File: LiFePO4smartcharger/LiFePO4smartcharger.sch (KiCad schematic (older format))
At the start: 96 parts, among them J1 Conn_01x02, J10 Conn_01x01, J11 Conn_01x01, J12 Conn_01x04, J2 Conn_02x03_Odd_Even, J3 Conn_01x02, J4 Conn_01x02, J5 Barrel_Jack, J6 Conn_01x01, J7 Conn_01x01, J8 Conn_01x02, J9 Conn_01x02, Q1 TIP42, Q2 TIP41, Q4 TIP41C, T1 Transformer_1P1Sdotted, U1 ATMEGA328P-PU, U2 LM358, U3 LCD-016N002L, U4 TL494, U9 LM7805_TO220, X3 16MHz

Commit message: Added important shutdown feature
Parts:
- added D8: 1N4148, Diodes_THT:D_DO-35_SOD27_P7.62mm_Horizontal, symbol D
- D4: footprint (none) -> Diodes_THT:D_DO-41_SOD81_P7.62mm_Horizontal
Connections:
- net CURRENTSHUNT: now also T1.2 (AB); no longer T1.4 (SB)
- net GND: now also T1.1 (AA); no longer T1.2 (AB)
- net SHUTDOWN: now reaches U1.6 ((PCINT20/XCK/T0)PD4)
- net SHUTDOWN: now also D8.2 (A)
- net at C9.1, J1.1 (Pin_1), J3.1 (Pin_1): now also T1.4 (SB); no longer T1.3 (SA)
- net at C10.2, R11.2, R15.1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: now also D8.1 (K)
- net at C13.1, C8.1, D4.1 (K)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: now also T1.3 (SA); no longer T1.1 (AA)
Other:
- moved on the sheet: C15, C16, T1

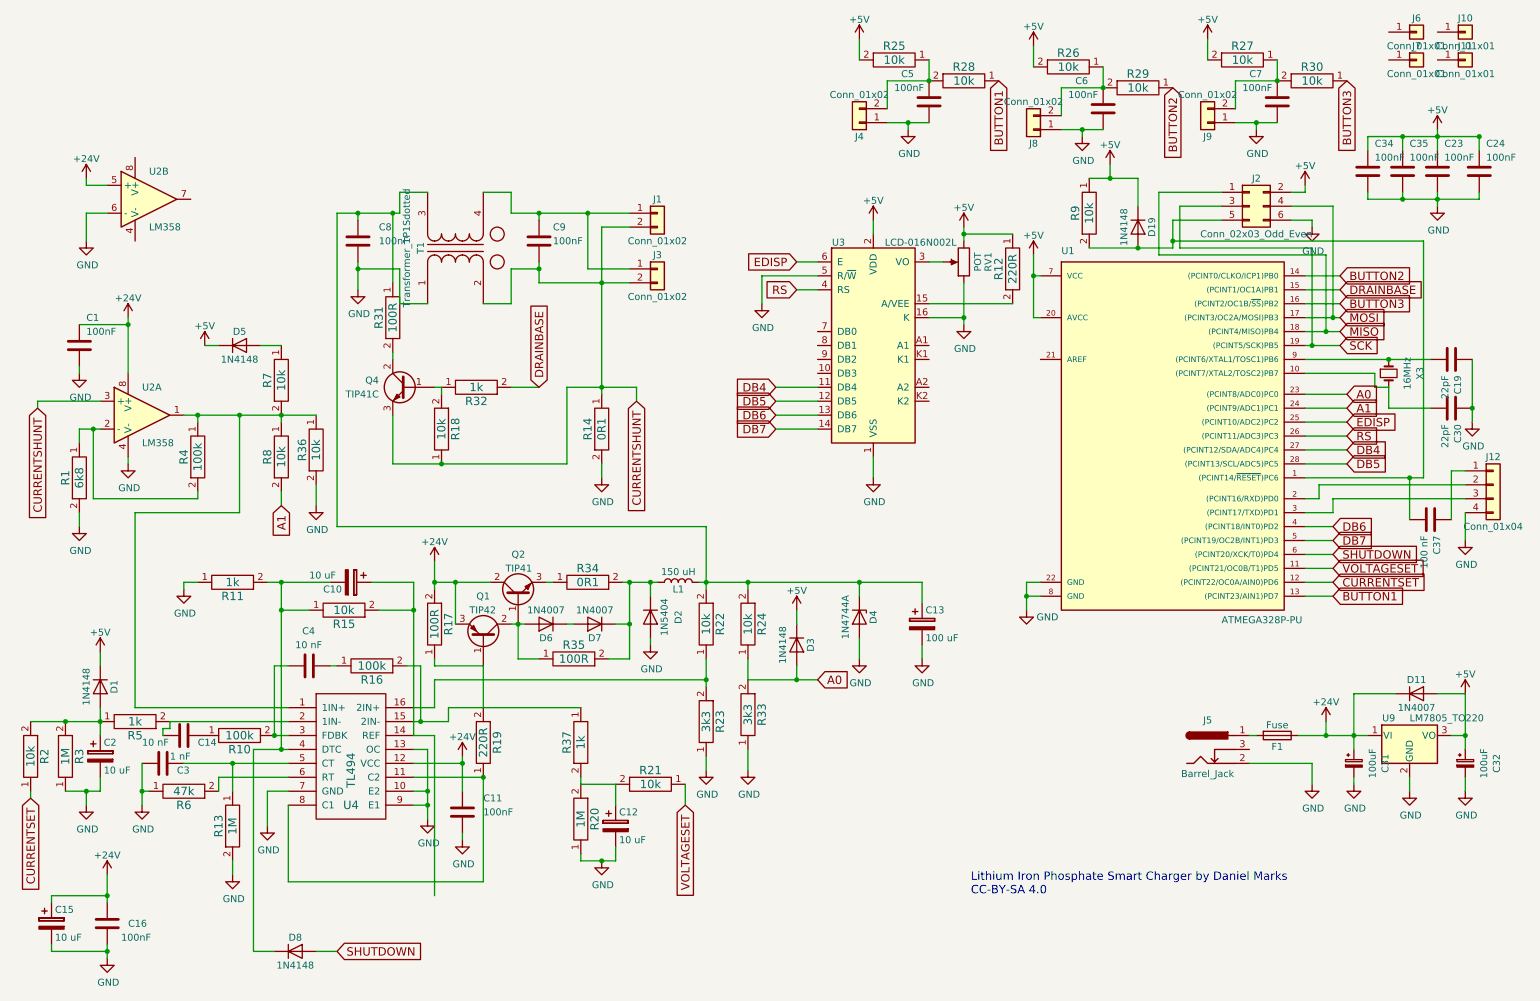
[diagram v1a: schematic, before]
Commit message: Changed to pulse to pulse shut off
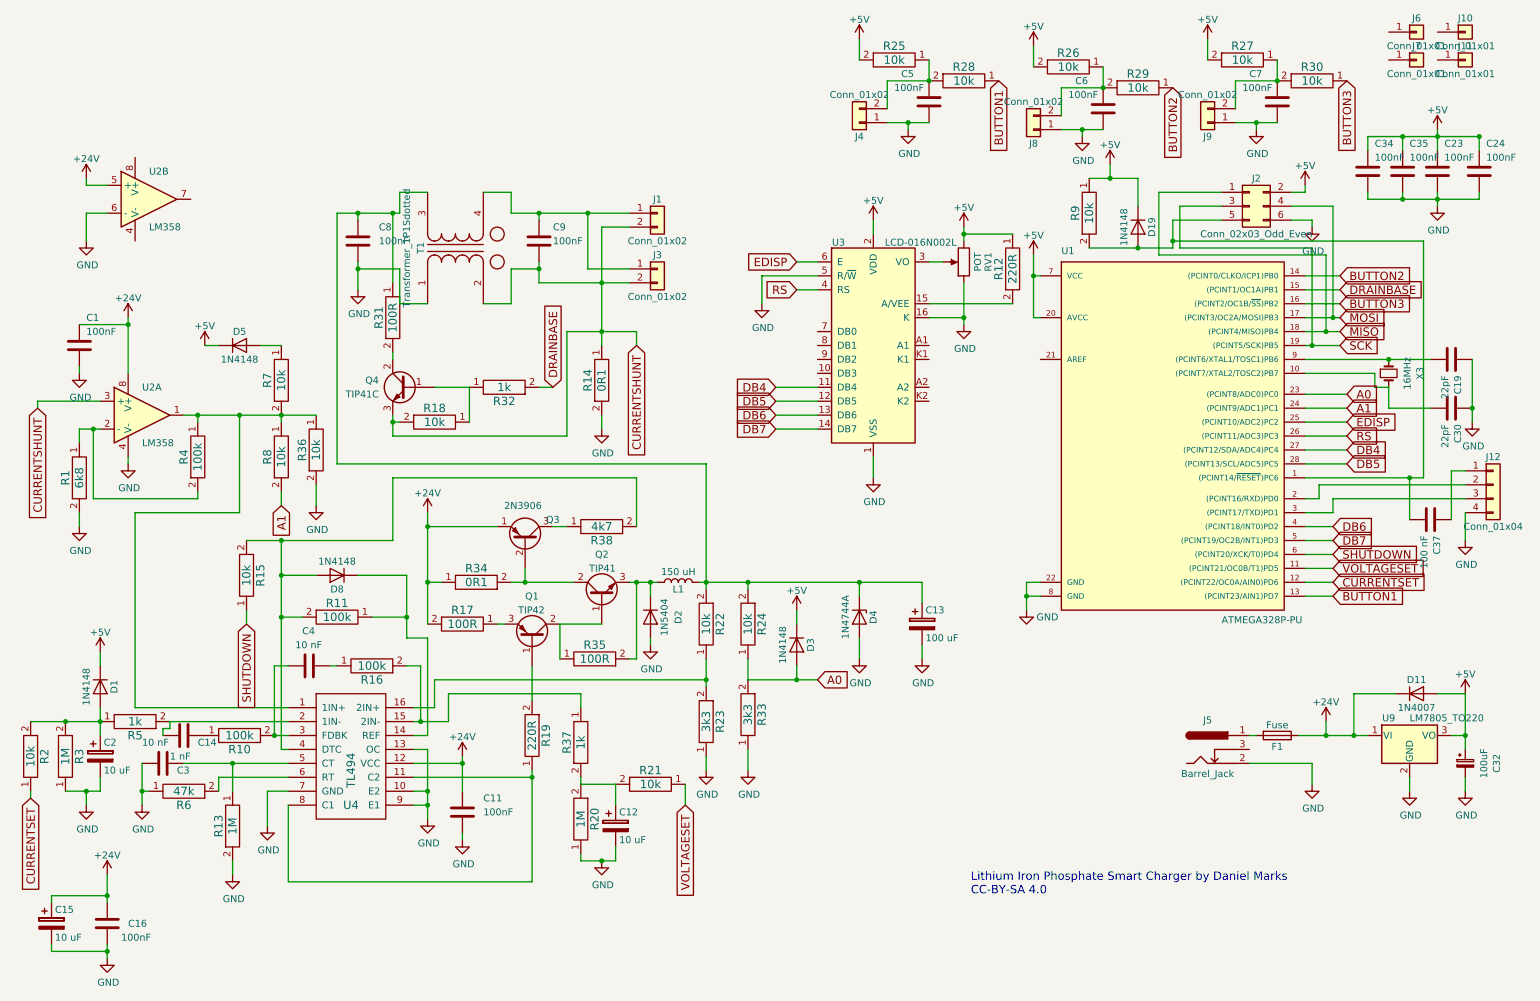
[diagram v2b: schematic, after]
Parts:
- removed C10: 10 uF, Capacitors_THT:CP_Radial_D5.0mm_P2.50mm, symbol CP
- removed C31: 100uF, Capacitors_THT:CP_Radial_D8.0mm_P3.50mm, symbol CP_Small
- removed D6, D7: 1N4007, Diodes_THT:D_DO-41_SOD81_P7.62mm_Horizontal, symbol D
- added Q3: 2N3906, TO_SOT_Packages_THT:TO-92_Inline_Wide, symbol 2N3906
- added R38: 4k7, Resistors_THT:R_Axial_DIN0207_L6.3mm_D2.5mm_P7.62mm_Horizontal, symbol RES
- R11: value 1k -> 100k
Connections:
- net +24V: now also R34.1, Q3.1 (E); no longer Q1.3 (E), Q2.2 (C)
- net CURRENTSHUNT: now also R18.2; no longer R18.1
- net GND: no longer R11.1
- net SHUTDOWN: now also R15.1; no longer D8.2 (A)
- net at U4.14 (REF): now also D8.1 (K), R11.1; no longer R15.2
- net at R11.2, U4.4 (DTC): now also D8.2 (A), R15.2, R38.2; no longer D8.1 (K), R15.1
- net at Q1.1 (B), R19.2: no longer R17.1
- net at Q2.3 (E): now also D2.1 (K), L1.1, R35.2; no longer R34.1
- net at Q4.1 (B), R32.1: now also R18.1; no longer R18.2
- new net: Q1.3 (E), R17.1
- new net: Q2.2 (C), Q3.2 (B), R34.2
- new net: Q3.3 (C), R38.1
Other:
- moved on the sheet: D8, Q1, Q2, R11, R14, R17, R18, R19, R32, R34, R35

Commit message: Oops moved resistor in TIP42
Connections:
- net +24V: no longer R17.2
- net at Q1.1 (B), R19.2: now also R17.1
- net at Q1.3 (E): now also Q2.2 (C), Q3.2 (B), R17.2, R34.2; no longer R17.1
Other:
- moved on the sheet: R17, R34

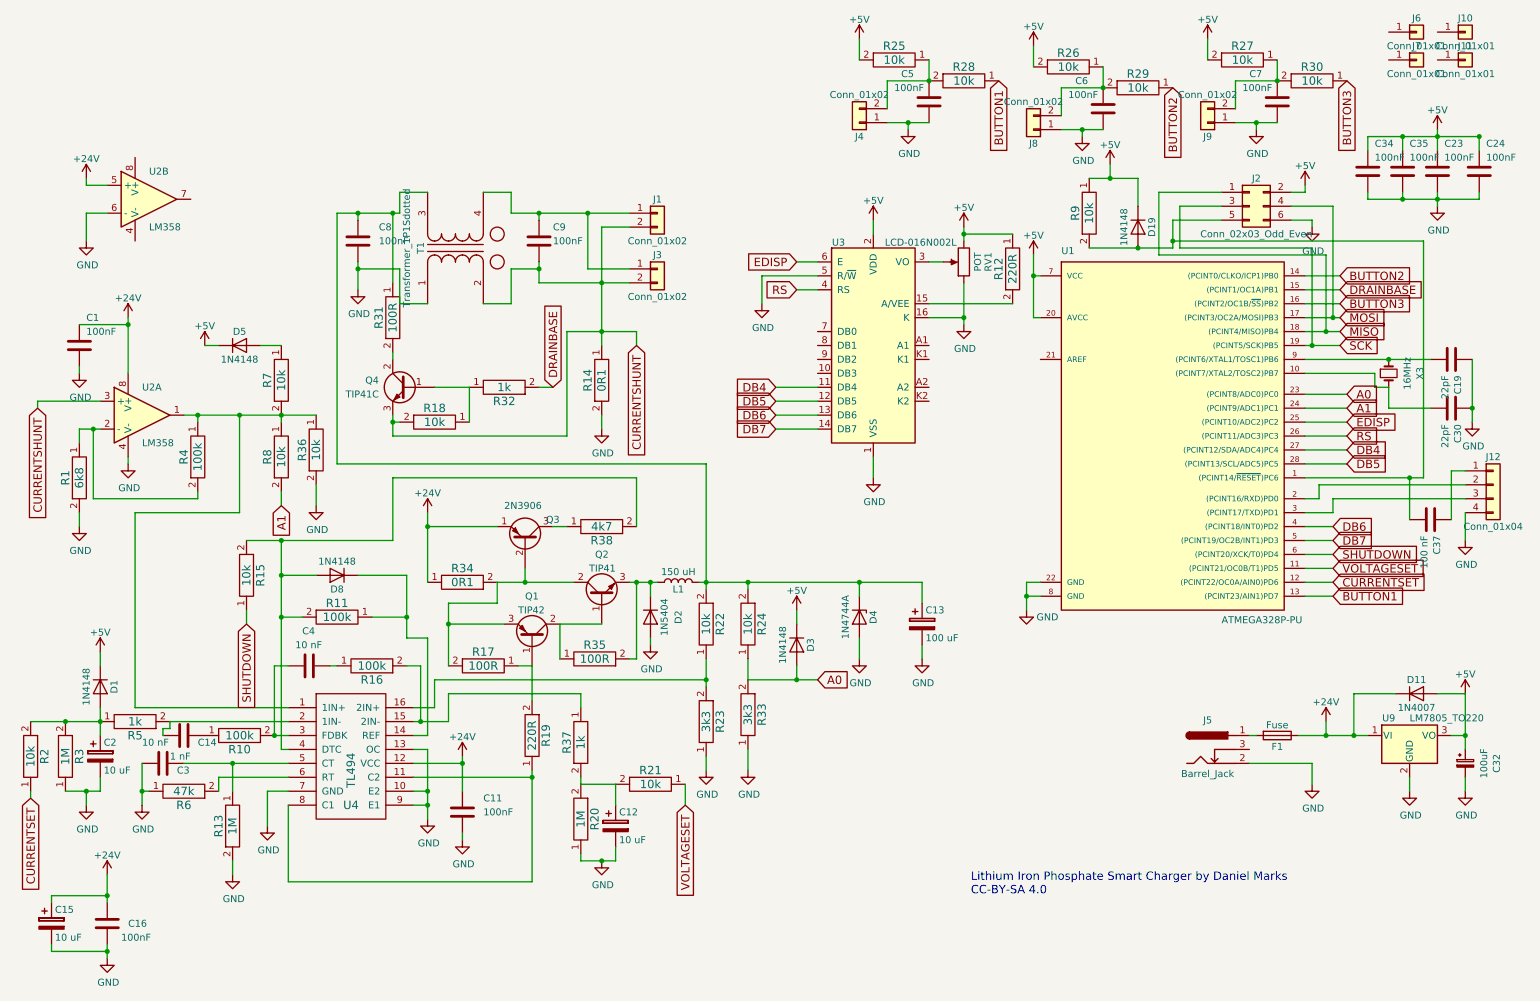
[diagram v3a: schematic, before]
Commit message: Cleaned up layout
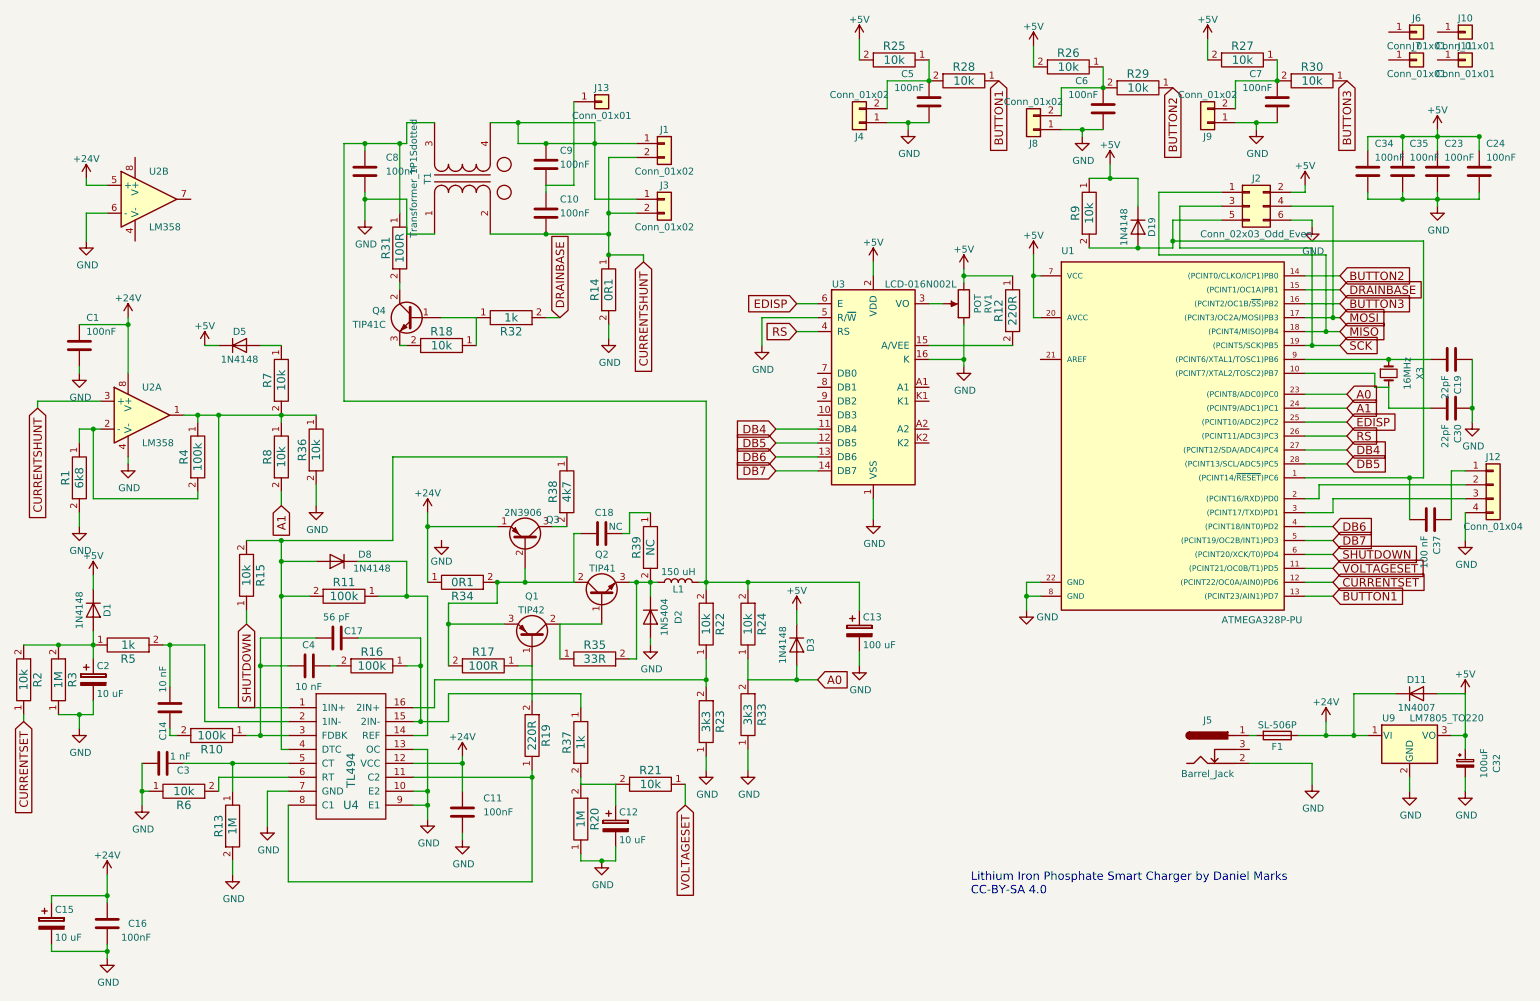
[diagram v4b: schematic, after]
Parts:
- removed D4: 1N4744A, Diodes_THT:D_DO-41_SOD81_P7.62mm_Horizontal, symbol D_Zener
- added C10: 100nF, Capacitors_THT:C_Disc_D5.0mm_W2.5mm_P5.00mm, symbol C
- added C17: 56 pF, Capacitors_THT:C_Disc_D5.0mm_W2.5mm_P5.00mm, symbol C
- added C18: NC, Capacitors_THT:C_Disc_D5.0mm_W2.5mm_P5.00mm, symbol C
- added J13: Conn_01x01, Connectors:1pin, symbol Conn_01x01
- added R39: NC, Resistors_THT:R_Axial_DIN0207_L6.3mm_D2.5mm_P7.62mm_Horizontal, symbol RES
- D8: footprint Diodes_THT:D_DO-35_SOD27_P7.62mm_Horizontal -> Diodes_THT:D_DO-41_SOD81_P7.62mm_Horizontal
- F1: value Fuse -> SL-506P
- R35: value 100R -> 33R
- R6: value 47k -> 10k
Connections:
- net CURRENTSHUNT: now also C10.2; no longer C9.2, Q4.3 (E), R18.2
- net at R37.1, U4.15 (2IN-): now also R16.1, C17.1; no longer R16.2
- net at C4.2, U4.3 (FDBK): now also R10.1, C17.2; no longer R10.2
- net at D8.2 (A), R11.2, R15.2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: now also R38.1; no longer R38.2
- net at Q1.3 (E), Q2.2 (C), Q3.2 (B)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: now also C18.2
- net at D2.1 (K), L1.1, Q2.3 (E)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: now also R39.2
- net at C14.1: now also R10.2; no longer R10.1
- net at Q3.3 (C): now also R38.2; no longer R38.1
- net at C4.1: now also R16.2; no longer R16.1
- new net: C10.1, C9.2, J13.1 (Pin_1)
- new net: C18.1, R39.1
- new net: Q4.3 (E), R18.2
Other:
- moved on the sheet: C13, C14, C2, C8, C9, D1, D8, J1, J3, Q4, R10, R11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

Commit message: Cleaned up the layout more
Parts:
- D1, D3, D5: value 1N4148 -> 1N5819; footprint Diodes_THT:D_DO-35_SOD27_P7.62mm_Horizontal -> Diodes_THT:D_DO-41_SOD81_P7.62mm_Horizontal
- D8: value 1N4148 -> 1N5819
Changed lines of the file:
@@
 P 2100 3000
 F 0 "D5" H 2100 3100 50  0000 C CNN
-F 1 "1N4148" H 2100 2900 50  0000 C CNN
-F 2 "Diodes_THT:D_DO-35_SOD27_P7.62mm_Horizontal" H 2100 3000 50  0001 C CNN
+F 1 "1N5819" H 2100 2900 50  0000 C CNN
+F 2 "Diodes_THT:D_DO-41_SOD81_P7.62mm_Horizontal" H 2100 3000 50  0001 C CNN
 F 3 "" H 2100 3000 50  0001 C CNN
 	1    2100 3000
@@
 P 1050 4900
 F 0 "D1" H 1050 5000 50  0000 C CNN
-F 1 "1N4148" H 1050 4800 50  0000 C CNN
-F 2 "Diodes_THT:D_DO-35_SOD27_P7.62mm_Horizontal" H 1050 4900 50  0001 C CNN
+F 1 "1N5819" H 1050 4800 50  0000 C CNN
+F 2 "Diodes_THT:D_DO-41_SOD81_P7.62mm_Horizontal" H 1050 4900 50  0001 C CNN
 F 3 "" H 1050 4900 50  0001 C CNN
 	1    1050 4900
@@
 L +5V #PWR043
 U 1 1 6046C7B3
-P 1050 4650
-F 0 "#PWR043" H 1050 4500 50  0001 C CNN
-F 1 "+5V" H 1050 4790 50  0000 C CNN
-F 2 "" H 1050 4650 50  0001 C CNN
-F 3 "" H 1050 4650 50  0001 C CNN
-	1    1050 4650
+P 1050 4750
+F 0 "#PWR043" H 1050 4600 50  0001 C CNN
+F 1 "+5V" H 1050 4890 50  0000 C CNN
+F 2 "" H 1050 4750 50  0001 C CNN
+F 3 "" H 1050 4750 50  0001 C CNN
+	1    1050 4750
 	1    0    0    -1
 $EndComp
@@
 P 6100 5150
 F 0 "D3" H 6100 5250 50  0000 C CNN
-F 1 "1N4148" H 6100 5050 50  0000 C CNN
-F 2 "Diodes_THT:D_DO-35_SOD27_P7.62mm_Horizontal" H 6100 5150 50  0001 C CNN
+F 1 "1N5819" H 6100 5050 50  0000 C CNN
+F 2 "Diodes_THT:D_DO-41_SOD81_P7.62mm_Horizontal" H 6100 5150 50  0001 C CNN
 F 3 "" H 6100 5150 50  0001 C CNN
 	1    6100 5150
@@
 P 2800 4550
 F 0 "D8" H 2600 4500 50  0000 C CNN
-F 1 "1N4148" H 2550 4600 50  0000 C CNN
+F 1 "1N5819" H 2550 4600 50  0000 C CNN
 F 2 "Diodes_THT:D_DO-41_SOD81_P7.62mm_Horizontal" H 2800 4550 50  0001 C CNN
 F 3 "" H 2800 4550 50  0001 C CNN
@@
 	550  5150 1050 5150
 Wire Wire Line
-	1050 4650 1050 4750
+	1050 4750 1050 4750
 Wire Wire Line
 	2400 5900 2450 5900

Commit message: A few tweaks
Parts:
- added R40: 10k, Resistors_THT:R_Axial_DIN0207_L6.3mm_D2.5mm_P7.62mm_Horizontal, symbol RES
- D2: value 1N5404 -> SB580
- R19: footprint Resistors_THT:R_Axial_DIN0207_L6.3mm_D2.5mm_P7.62mm_Horizontal -> Resistors_THT:R_Axial_DIN0309_L9.0mm_D3.2mm_P12.70mm_Horizontal
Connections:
- net CURRENTSHUNT: now also Q4.1 (B), R18.1, R32.1
- net at C18.2, Q1.3 (E), Q2.2 (C)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: now also R40.1; no longer Q3.2 (B)
- new net: Q3.2 (B), R40.2
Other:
- moved on the sheet: C13, D3, D5, Q3, R22, R23, R24, R33, R38, R7, R8
